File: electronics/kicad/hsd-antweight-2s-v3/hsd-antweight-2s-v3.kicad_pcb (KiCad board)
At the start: 2 copper layers, 78 x 56 mm, 10 parts, among them J10 3V3 GND VLIPO, J4 BATTERY, J5 MOTOR LEFT, J6 MOTOR RIGHT, SW1 SW EXT VBAT_RAW/VBAT_SW, U1 ESP32-C3 SUPERMINI, U2 DRV8833, U3 EXT REG LOGIC VIN GND VOUT

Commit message: kicad v3: save latest pcb update
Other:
- board size 78 x 56 mm -> 78.1 x 56 mm
- board text added: "E"
- board text added: "V"
- board text removed: "VE"

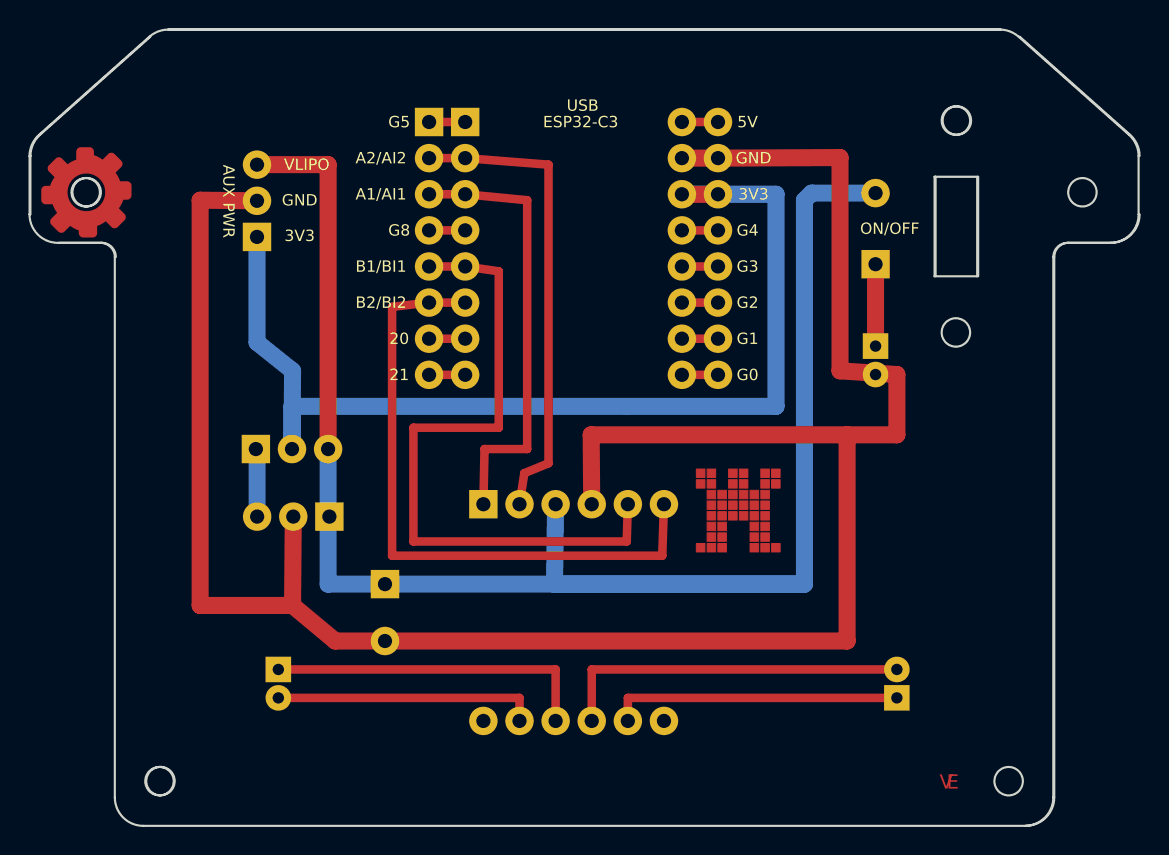
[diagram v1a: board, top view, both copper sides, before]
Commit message: Sync v3 folder with latest v3 PCB design outputs
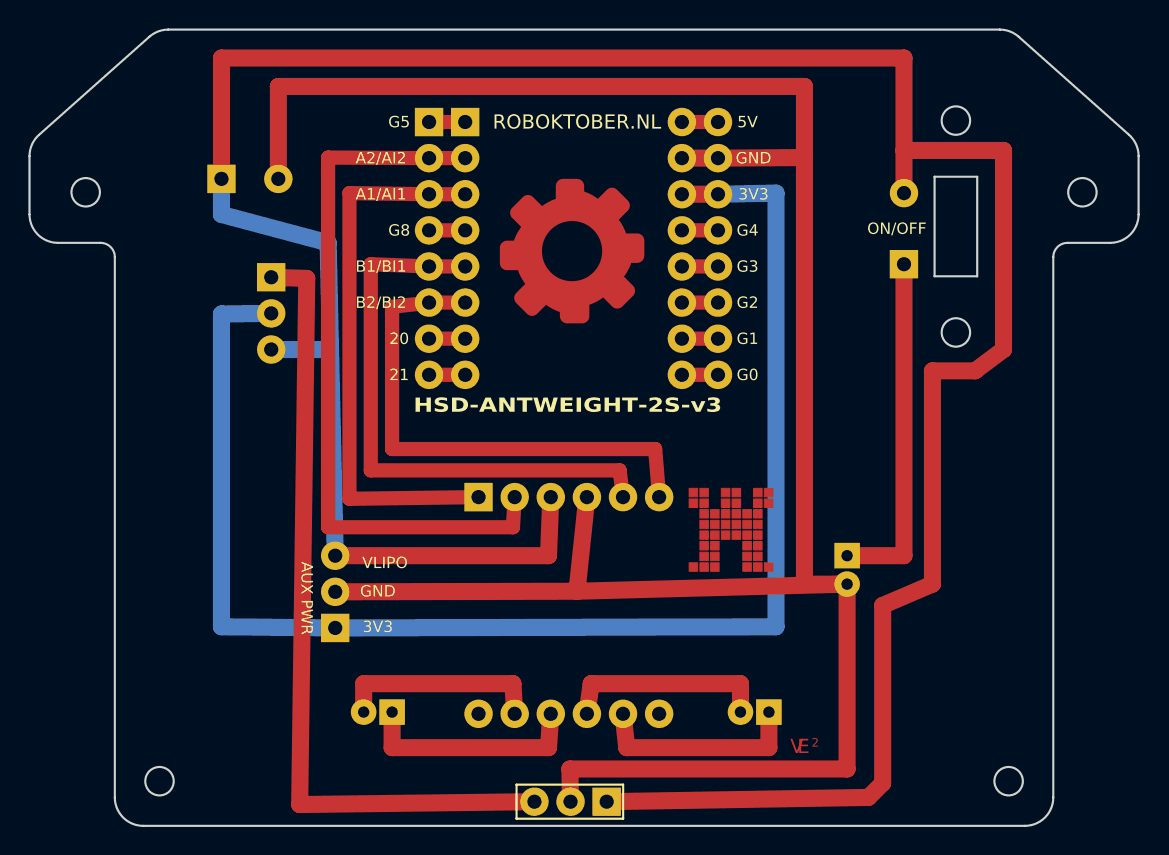
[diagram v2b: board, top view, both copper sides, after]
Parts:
- moved C1_C2 30.7 mm to (33.0, 39.5), turned to 0 degrees
- moved J10 28.0 mm to (41.0, 71.1)
- moved U3 28.0 mm to (60.1, 83.3)
- moved J4 14.9 mm to (77.0, 66.0)
- moved JP1 12.1 mm to (36.5, 46.4), turned to -90 degrees
- moved J5 9.06 mm to (71.5, 77.0), turned to 180 degrees
- moved J6 8.54 mm to (45.0, 77.0), turned to 180 degrees
- moved SW1 2.00 mm to (81.0, 45.5)
- moved U2 0.60 mm to (51.1, 77.1)
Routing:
- net VBAT_SW: track 123.6 -> 199.4 mm
- net REG_3V3_2S: track 4.84 -> 56.1 mm
- net 3V3: track 77.2 -> 101.6 mm
- net VBAT_RAW: track 6.00 -> 24.7 mm
- net AIN2_GPIO6: track 33.5 -> 50.8 mm
- net M1B: track 25.1 -> 14.6 mm
- net BIN2_GPIO10: track 45.7 -> 37.4 mm
- net AIN1_GPIO7: track 31.3 -> 38.7 mm
- net M2A: track 23.1 -> 15.9 mm
- net GND: track 160.4 -> 167.6 mm
- net BIN1_GPIO9: track 47.5 -> 40.5 mm
- net M1A: track 20.5 -> 14.9 mm
- net M2B: track 18.6 -> 14.6 mm
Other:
- board size 78.1 x 56 mm -> 78 x 56 mm
- board text added: "1S/3.7V"
- board text added: "2"
- board text added: "2S/7.4V"
- board text added: "HSD-ANTWEIGHT-2S-v3"
- board text added: "VIN"
- board text removed: "BYPASS"
- board text removed: "JP1 SEL: 2S=1-2 | 1S=2-3"
- board text removed: "USB"

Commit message: Update v3 PCB assets and rerender outputs
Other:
- board text added: "DRENTHE"
- board text added: "HACKERSPACE"
- board text added: "Online"
- board text added: "Wallie"
